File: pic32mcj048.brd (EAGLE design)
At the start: 100 x 80 mm, 1 part

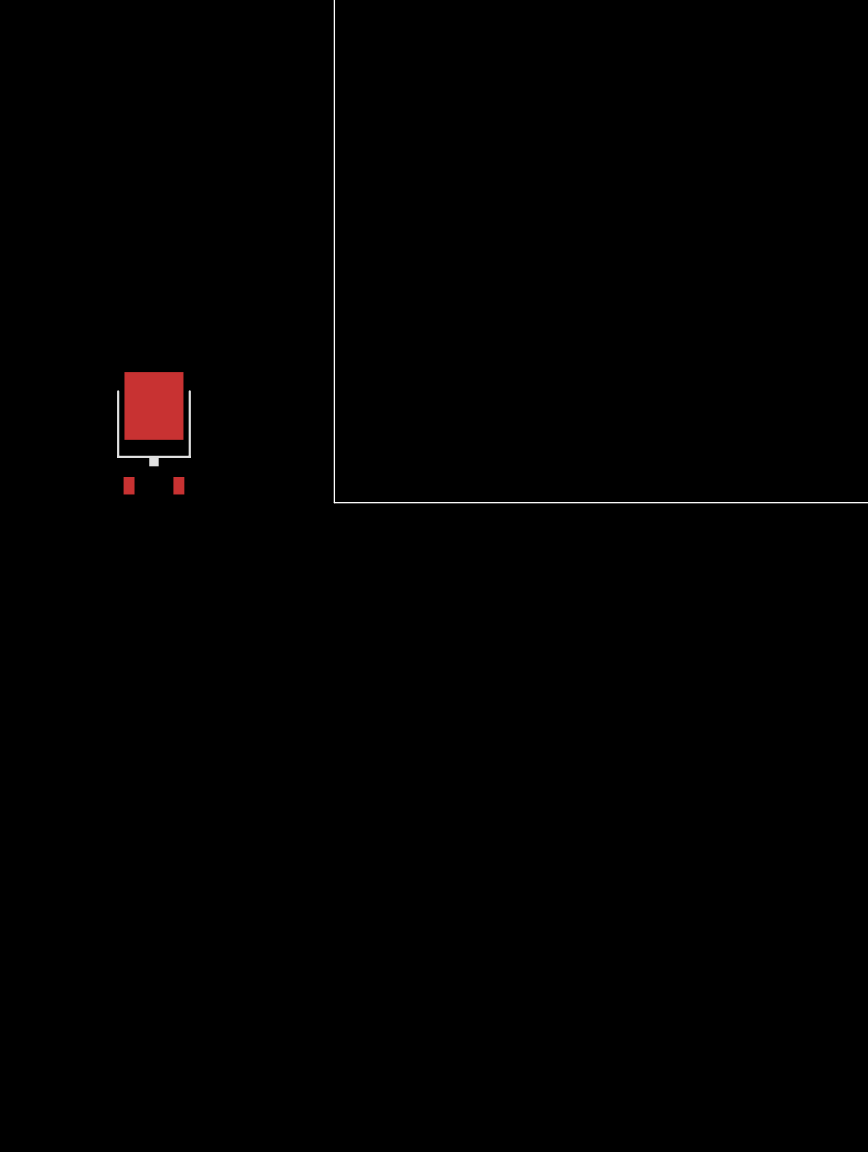
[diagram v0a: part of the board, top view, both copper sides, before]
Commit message: リセット回路、書き込み回路を作った
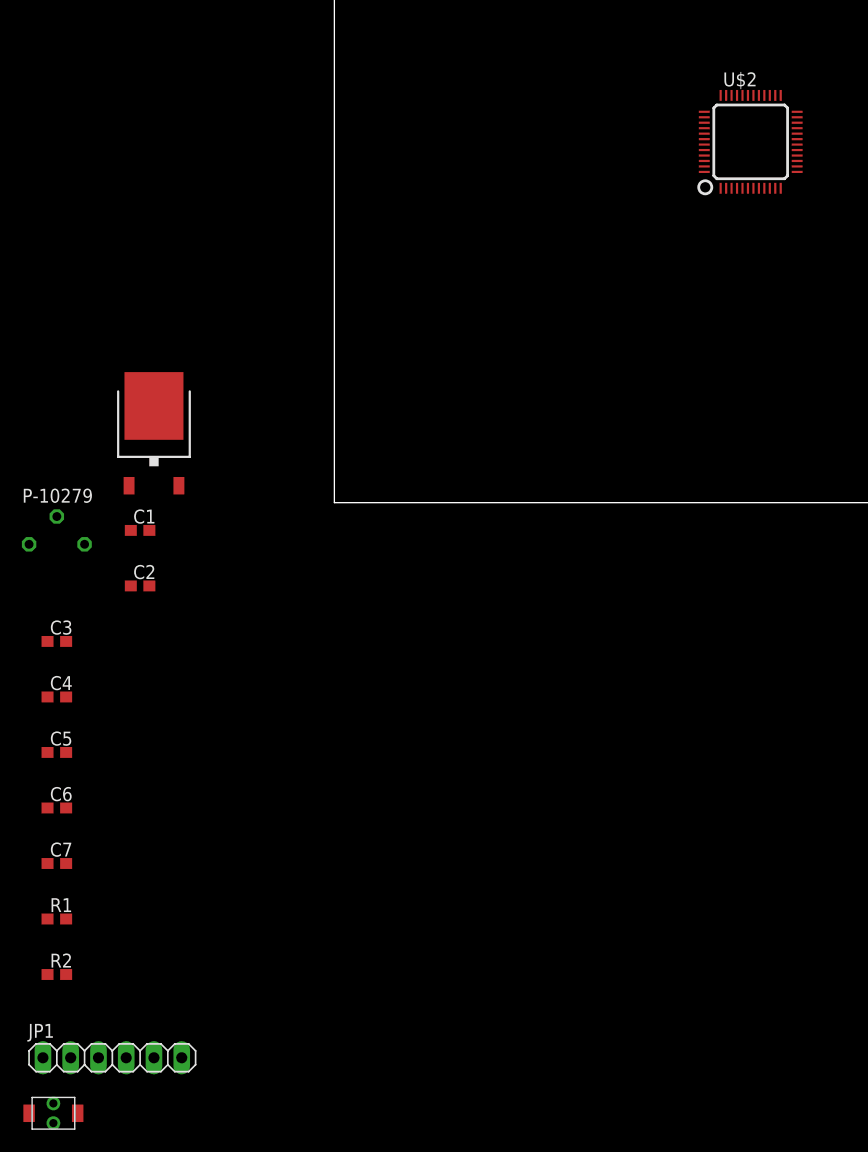
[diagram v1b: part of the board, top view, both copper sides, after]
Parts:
- added C1: 0.47u, rcl:C1608
- added C2: 10u, rcl:C1608
- added C3, C4, C5, C6, C7: 0.1u, rcl:C1608
- added JP1: (no value), pinhead:1X06
- added P-10279: (no value), user_emifilter:LCL
- added R1: 10k, user_rcl:1608
- added R2: 1k, user_rcl:1608
- added U$2: PIC32MK0512MCJ048, user_ic:LQFP48PIN
- added U$3: TAKUTOSUITTI2, user_swich:TAKUTOSUITTI2
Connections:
- new net 3.3V: C3.2, C4.1, C5.2, C6.1, JP1.4, P-10279.2, R1.2, U$2.PIN15, U$2.PIN26, U$2.PIN43, U$2.PIN6
- new net GND: C1.2, C2.2, C3.1, C4.2, C5.1, C6.2, C7.2, JP1.5, P-10279.0, U$1.PIN2, U$2.PIN16, U$2.PIN29, U$2.PIN42, U$2.PIN5, U$3.P$1
- new net MCLR: JP1.1, R2.2, U$2.PIN4
- new net N$1: C2.1, P-10279.1, U$1.PIN3
- new net N$2: C7.1, R1.1, R2.1, U$3.P$2
- new net PGC: JP1.2, U$2.PIN32
- new net PGD: JP1.3, U$2.PIN31
- new net VCC: C1.1, U$1.PIN1

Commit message: brdfileを編集
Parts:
- moved JP1 135.4 mm to (33.0, 73.7), turned to 180 degrees
- moved U$3 119.2 mm to (32.4, 46.9), turned to 180 degrees
- moved R2 111.5 mm to (30.5, 53.3), turned to 90 degrees
- moved C6 109.5 mm to (40.6, 59.5), turned to 90 degrees
- moved C5 109.5 mm to (34.5, 68.8)
- moved R1 105.9 mm to (27.9, 53.3), turned to 90 degrees
- moved C7 99.3 mm to (28.8, 50.2)
- moved C4 93.7 mm to (25.4, 61.0), turned to 90 degrees
- moved C3 88.2 mm to (33.0, 53.3), turned to 90 degrees
- moved C1 71.6 mm to (39.0, 41.0), turned to 270 degrees
- moved C2 67.9 mm to (29.6, 41.0), turned to 270 degrees
- moved P-10279 65.0 mm to (27.1, 35.8), turned to 270 degrees
- moved U$1 59.2 mm to (34.3, 36.8), turned to 180 degrees
- moved U$2 28.4 mm to (33.0, 61.0)
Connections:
- net 3.3V: now also JP1.2; no longer JP1.4
- net GND: now also JP1.3; no longer JP1.5
- net PGC: now also JP1.5; no longer JP1.2
- net PGD: now also JP1.4; no longer JP1.3
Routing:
- net 3.3V: track 0.00 -> 104.4 mm
- net GND: track 0.00 -> 31.6 mm
- net MCLR: track 0.00 -> 23.2 mm, vias 0 -> 1
- net PGC: track 0.00 -> 9.72 mm
- net PGD: track 0.00 -> 8.87 mm
- net N$1: track 0.00 -> 8.71 mm
- net N$2: track 0.00 -> 8.10 mm
- net VCC: track 0.00 -> 2.54 mm

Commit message: sch完成
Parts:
- added C10, C11: 22p, rcl:C1608
- added C8: 0.1u, rcl:C1608
- added C9: 10u, rcl:C1608
- added IC1: (no value), user_ic:DIL8
- added JP2, JP3: (no value), pinhead:1X15
- added OSC1: 16M, user_osc:CSTNE#
- added R3, R4, R5, R6: 10k, user_rcl:1608
- added R7: 1k, user_rcl:1608
- added R8: (no value), user_rcl:1608
- added R_I1: 4.7k, user_rcl:1005X4RESISTOR
- added U$5: RGB_LED, user_leds:RGB_LED
- added U$6: FDC6305, user_tr_fet_igbt:SSOT6
- added U$7: NJM2380, user_ic:SOT23-5
- added X1: 32.768k, user_osc:FC255
- moved C5 11.6 mm to (34.5, 57.2)
- moved C3 10.2 mm to (33.0, 43.2)
- moved C4 10.2 mm to (25.4, 50.8)
- moved C6 10.2 mm to (40.6, 49.3)
- moved C7 10.2 mm to (28.8, 40.0)
- moved P-10279 10.2 mm to (27.1, 25.7)
- moved R1 10.2 mm to (27.9, 43.2)
- moved R2 10.2 mm to (30.5, 43.2)
- moved U$2 10.2 mm to (33.0, 50.8)
- moved C1 10.2 mm to (39.0, 30.9)
- moved C2 10.2 mm to (29.6, 30.8)
- moved U$1 10.2 mm to (34.3, 26.7)
- moved U$3 10.2 mm to (32.4, 36.8)
- moved JP1 2.54 mm to (33.0, 76.2)
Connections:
- new net C1RX: IC1.PIN4, U$2.PIN25
- new net C1TX: IC1.PIN1, U$2.PIN34
- new net CANH: IC1.PIN6, JP3.9
- new net CANL: IC1.PIN7, JP3.10
- new net LED_G: U$2.PIN33, U$6.1
- new net LED_R: U$2.PIN30, U$6.3
- new net N$11: R8.1, U$2.PIN36
- new net N$13: R4.1, U$5.B_A
- new net N$14: R5.1, U$5.G_A
- new net N$15: R6.1, U$5.R_A
- new net N$21: R_I1.7, R_I1.8, U$7.5
- new net N$3: OSC1.P$1, U$2.PIN28
- new net N$4: OSC1.P$3, U$2.PIN27
- new net N$45: R_I1.2, R_I1.3
- new net N$46: R_I1.5, R_I1.6
- new net N$5: IC1.PIN5, R3.1
- new net N$6: C10.1, R8.2, X1.P$2
- new net N$7: C11.1, U$2.PIN35, X1.P$1
- new net N$8: U$5.G_K, U$6.6
- new net N$9: U$5.R_K, U$6.4
- new net RA0: U$2.PIN9
- new net RA1: U$2.PIN10
- new net RA10: JP2.10, U$2.PIN48
- new net RA11: U$2.PIN8
- new net RA12: U$2.PIN7
- new net RA7: U$2.PIN1
- new net RA8: JP3.2, U$2.PIN23
- new net RB10: JP2.6, U$2.PIN44
- new net RB11: JP2.7, U$2.PIN45
- new net RB12: JP2.8, U$2.PIN46
- new net RB13: JP2.9, U$2.PIN47
- new net RB14: U$2.PIN2
- new net RB15: U$2.PIN3
- new net RB2: JP3.8, U$2.PIN13
- new net RB3: JP3.7, U$2.PIN14
- new net RB4: JP3.1, U$2.PIN24
- new net RB9: JP2.1, U$2.PIN37
- new net RC0: JP3.6, U$2.PIN17
- new net RC1: JP3.5, U$2.PIN18
- new net RC11: JP3.3, U$2.PIN20
- new net RC2: JP3.4, U$2.PIN19
- new net RC6: JP2.2, U$2.PIN38
- new net RC7: JP2.3, U$2.PIN39
- new net RC8: JP2.4, U$2.PIN40
- new net RC9: JP2.5, U$2.PIN41
- new net VREF+: C9.1, R7.1, R_I1.1, U$2.PIN12, U$7.4
- net 3.3V: now also C8.2, IC1.PIN8, JP2.11, JP3.11, R4.2, R5.2, R6.2, U$2.PIN22
- net GND: now also C10.2, C11.2, C8.1, C9.2, IC1.PIN2, JP2.12, JP2.14, JP3.12, JP3.14, OSC1.P$2, R_I1.4, U$2.PIN11, U$2.PIN21, U$5.B_K, U$6.2, U$6.5, U$7.2
- net VCC: now also IC1.PIN3, JP2.13, JP2.15, JP3.13, JP3.15, R3.2, R7.2
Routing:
- net 3.3V: track 104.4 -> 87.0 mm
- net MCLR: track 23.2 -> 35.9 mm
- net PGD: track 8.87 -> 21.6 mm
- net PGC: track 9.72 -> 22.4 mm
- net N$4: track 0.00 -> 7.55 mm, vias 0 -> 1
- net N$3: track 0.00 -> 6.60 mm, vias 0 -> 1
- net GND: track 31.6 -> 25.1 mm

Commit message: 基本設計完了、あとは調整など
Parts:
- added C12, C13: 0.1u, rcl:C1608
- added C14: 0.47u, rcl:C1608
- added R9: 120, user_rcl:1608
- added U$4: XH_2P, user_conector:XH_2P
- added U$8: NJM2391, user_ic:TO252
- R4, R5, R6: value 10k -> 1k
- moved R8 83.0 mm to (7.98, 28.1), flipped to the bottom, turned to 90 degrees
- moved C11 81.9 mm to (8.20, 32.0), turned to 90 degrees
- moved C10 76.4 mm to (6.13, 32.0), turned to 90 degrees
- moved IC1 73.3 mm to (14.7, 36.4)
- moved R6 71.7 mm to (5.13, 40.7), flipped to the bottom, turned to 270 degrees
- moved R5 67.9 mm to (7.17, 40.7), flipped to the bottom, turned to 270 degrees
- moved U$5 65.6 mm to (5.55, 35.6), turned to 90 degrees
- moved X1 64.6 mm to (10.5, 29.0), turned to 180 degrees
- moved R4 64.4 mm to (9.19, 40.7), flipped to the bottom, turned to 270 degrees
- moved U$6 63.6 mm to (7.68, 35.5), flipped to the bottom, turned to 270 degrees
- moved C8 58.1 mm to (15.4, 23.9), flipped to the bottom, turned to 90 degrees
- moved C9 54.0 mm to (16.4, 16.6), flipped to the bottom, turned to 180 degrees
- moved R3 53.2 mm to (18.3, 37.0), flipped to the bottom, turned to 270 degrees
- moved R7 45.4 mm to (13.6, 13.5), flipped to the bottom, turned to 270 degrees
- moved R_I1 41.4 mm to (15.8, 13.9), flipped to the bottom, turned to 180 degrees
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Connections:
- removed net CANH: IC1.PIN6, JP3.9
- removed net CANL: IC1.PIN7, JP3.10
- new net +5V: C1.1, C12.1, C13.1, IC1.PIN3, JP3.15, R3.2, R7.2, U$1.PIN1, U$8.PIN3
- new net CAN_N: IC1.PIN7, JP3.1, R9.1
- new net CAN_P: IC1.PIN6, JP3.2, R9.2
- net 3.3V: now also JP2.14; no longer JP2.11, JP3.11
- net GND: now also C12.2, C13.2, C14.2, JP2.15, U$4.P$1, U$8.PIN2; no longer JP2.12, JP2.14, JP3.12, JP3.14
- net RA0: now also JP3.12
- net RA1: now also JP3.11
- net RA11: now also JP3.13
- net RA12: now also JP3.14
- net RA7: now also JP2.11
- net RA8: now also JP3.4; no longer JP3.2
- net RB14: now also JP2.12
- net RB15: now also JP2.13
- net RB2: now also JP3.10; no longer JP3.8
- net RB3: now also JP3.9; no longer JP3.7
- net RB4: now also JP3.3; no longer JP3.1
- net RC0: now also JP3.8; no longer JP3.6
- net RC1: now also JP3.7; no longer JP3.5
- net RC11: now also JP3.5; no longer JP3.3
- net RC2: now also JP3.6; no longer JP3.4
- net VCC: now also C14.1, U$4.P$2, U$8.PIN1; no longer C1.1, IC1.PIN3, JP2.13, JP2.15, JP3.13, JP3.15, R3.2, R7.2, U$1.PIN1
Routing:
- net +5V: track 0.00 -> 59.6 mm, vias 0 -> 3
- net RB9: track 0.00 -> 22.9 mm, vias 0 -> 1
- net RA12: track 0.00 -> 18.4 mm
- net LED_G: track 0.00 -> 17.8 mm, vias 0 -> 1
- net RC6: track 0.00 -> 16.8 mm
- net RA11: track 0.00 -> 15.5 mm
- net RB15: track 0.00 -> 15.3 mm, vias 0 -> 1
- net RC7: track 0.00 -> 15.0 mm
- net CAN_N: track 0.00 -> 14.7 mm
- net CAN_P: track 0.00 -> 14.0 mm
- net RC8: track 0.00 -> 13.1 mm
- net RB4: track 0.00 -> 12.8 mm
- net RB14: track 0.00 -> 12.4 mm
- net RA0: track 0.00 -> 12.3 mm
- net LED_R: track 0.00 -> 12.1 mm, vias 0 -> 1
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- added copper zone on layer 1, net GND
- added copper zone on layer 16, net GND
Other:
- board size 100 x 80 mm -> 25.4 x 47 mm

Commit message: 完成、ガーバーデータ追加
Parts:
- moved R_I1 0.63 mm to (15.8, 14.5)
- moved U$7 0.63 mm to (16.8, 14.8)
- moved R2 0.10 mm to (8.87, 15.9)
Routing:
- net 3.3V: track 95.4 -> 132.7 mm
- net GND: track 18.1 -> 22.7 mm, vias 17 -> 64
- net RB9: track 22.9 -> 19.0 mm
- net MCLR: track 46.0 -> 49.0 mm
- net +5V: track 59.6 -> 62.2 mm, vias 3 -> 6
- net N$2: track 6.90 -> 5.84 mm
- net VREF+: track 7.40 -> 7.92 mm
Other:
- board text added: "3.3V"
- board text added: "5V"
- board text added: "CANH"
- board text added: "CANL"
- board text added: "GND"
- board text added: "MCLR"
- board text added: "NC"
- board text added: "PGC"
- board text added: "PGD"
- board text added: "RA0"
- board text added: "RA1"
- board text added: "RA10"
- board text added: "RA11"
- board text added: "RA12"
- board text added: "RA7"
- board text added: "RA8"
- board text added: "RB10"
- board text added: "RB11"
- board text added: "RB12"
- board text added: "RB13"
- board text added: "RB14"
- board text added: "RB15"
- board text added: "RB2"
- board text added: "RB3"
- board text added: "RB4"
- board text added: "RB9"
- board text added: "RC0"
- board text added: "RC1"
- board text added: "RC11"
- board text added: "RC2"
- board text added: "RC6"
- board text added: "RC7"
- board text added: "RC8"
- board text added: "RC9"

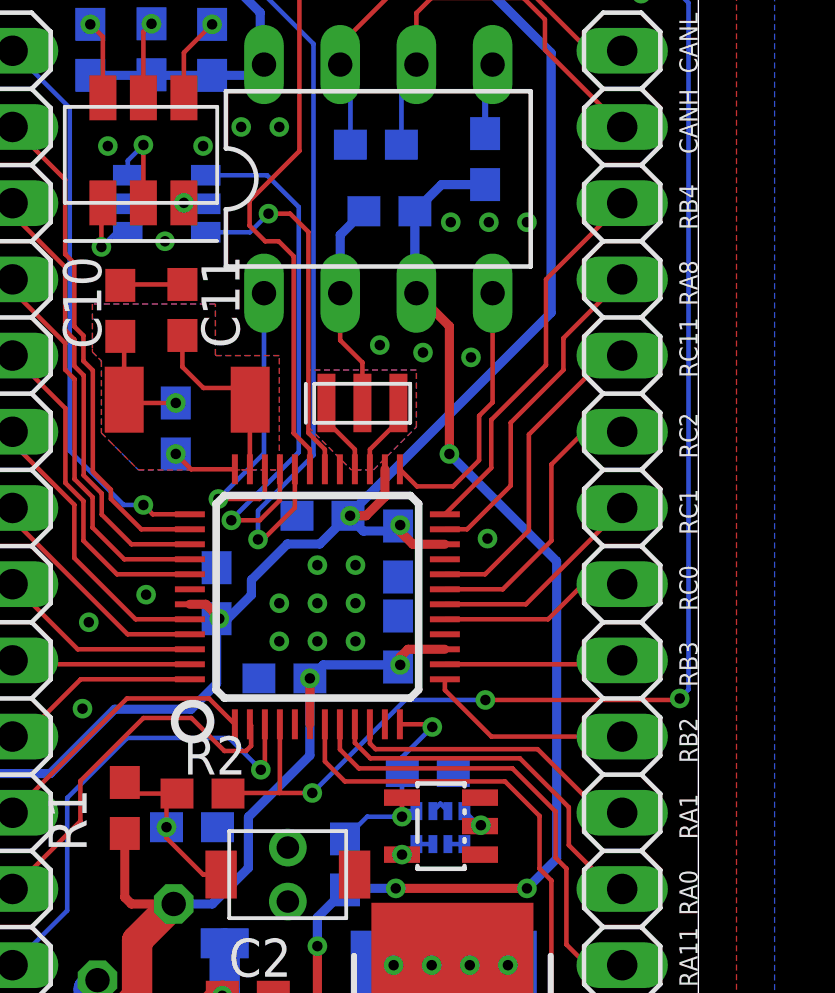
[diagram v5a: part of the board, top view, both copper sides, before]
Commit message: mcp2562スタンバイピンプルダウン
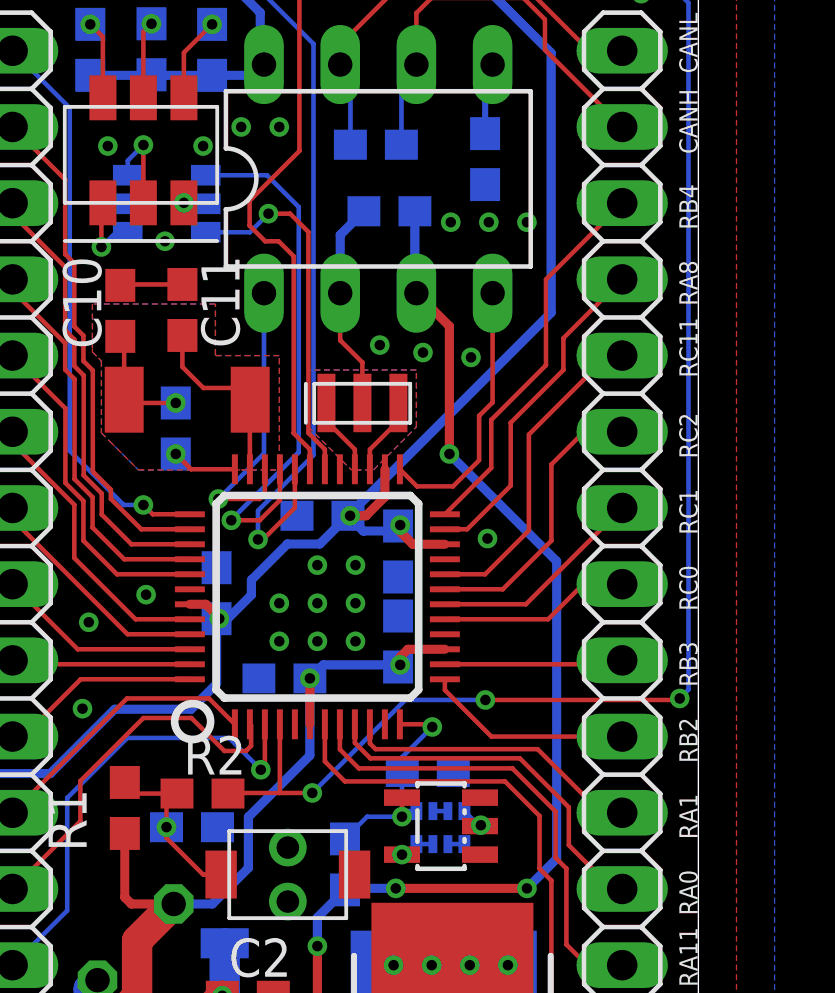
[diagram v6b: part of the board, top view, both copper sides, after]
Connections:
- net +5V: no longer R3.2
- net GND: now also R3.2
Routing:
- net +5V: track 62.2 -> 59.5 mm
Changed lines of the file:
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@@
 <via x="18.14926875" y="14.82426875" extent="1-16" drill="0.35"/>
 <via x="6.99" y="22.51" extent="1-16" drill="0.35"/>
+<contactref element="R3" pad="2"/>
 </signal>
 <signal name="VCC">
@@
 <contactref element="R_I1" pad="2"/>
 <contactref element="R_I1" pad="3"/>
-<wire x1="17.05" y1="15.295" x2="16.8" y2="15.545" width="0.1524" layer="16"/>
-<wire x1="16.8" y1="15.545" x2="16.55" y2="15.295" width="0.1524" layer="16"/>
+<wire x1="17.05" y1="15.295" x2="16.55" y2="15.295" width="0.1524" layer="16"/>
 </signal>
 <signal name="N$46">
@@
 <contactref element="C13" pad="1"/>
 <contactref element="R7" pad="2"/>
-<contactref element="R3" pad="2"/>
 <contactref element="IC1" pad="PIN3"/>
 <contactref element="C12" pad="1"/>
@@
 <wire x1="15.95" y1="35.29" x2="15.95" y2="32.61" width="0.3048" layer="16"/>
 <wire x1="15.95" y1="32.61" x2="16" y2="32.56" width="0.3048" layer="16"/>
-<wire x1="18.29" y1="36.18" x2="16.84" y2="36.18" width="0.3048" layer="16"/>
-<wire x1="16.84" y1="36.18" x2="15.95" y2="35.29" width="0.3048" layer="16"/>
 <contactref element="JP3" pad="15"/>
 <wire x1="19.48" y1="1.84" x2="22.72" y2="5.08" width="1.016" layer="1"/>
